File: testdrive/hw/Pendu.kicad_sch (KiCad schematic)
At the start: 26 parts, among them J2 Conn_01x04, J2 Conn_01x08, J3 Conn_01x05, J4 Conn_01x05, Q1 Si2301DS, SW1 Vib, U1 SPX3819M5-L-3-3, U2 STM32G030F6Px, U3 SPX3819M5-L-1-8, U4 BMI270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

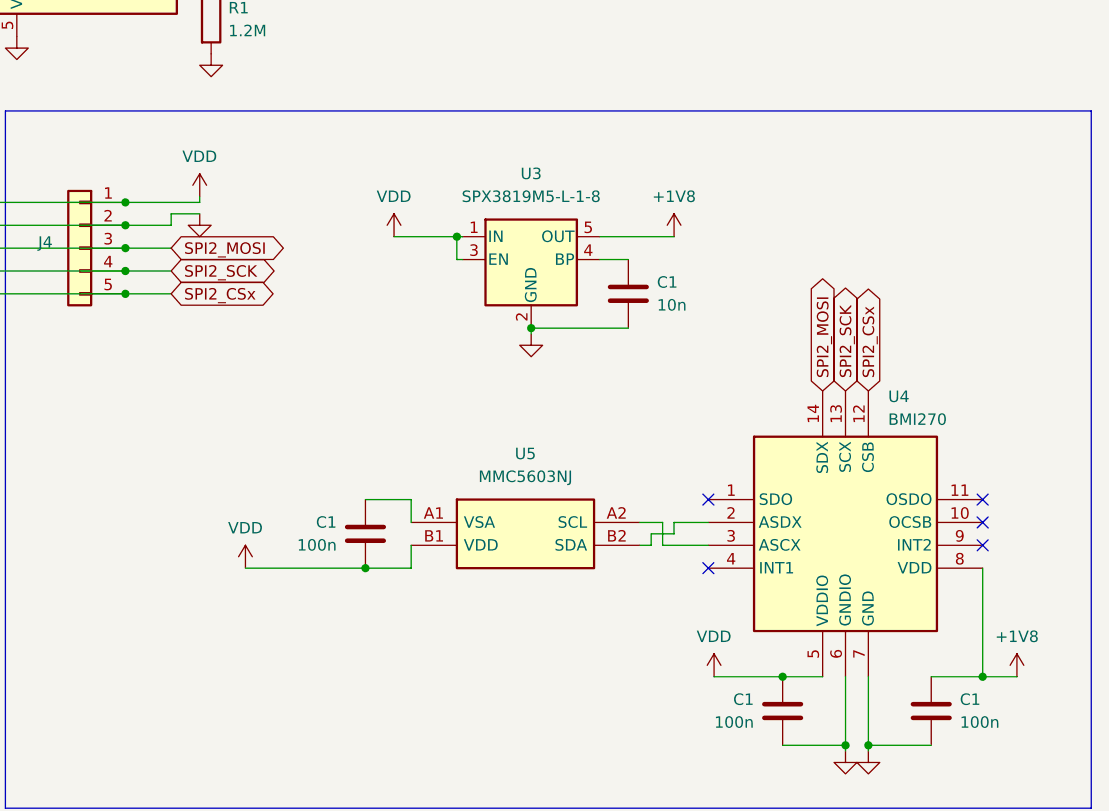
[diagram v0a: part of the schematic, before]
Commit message: Revise testdrive schematic, revert to unified VDD
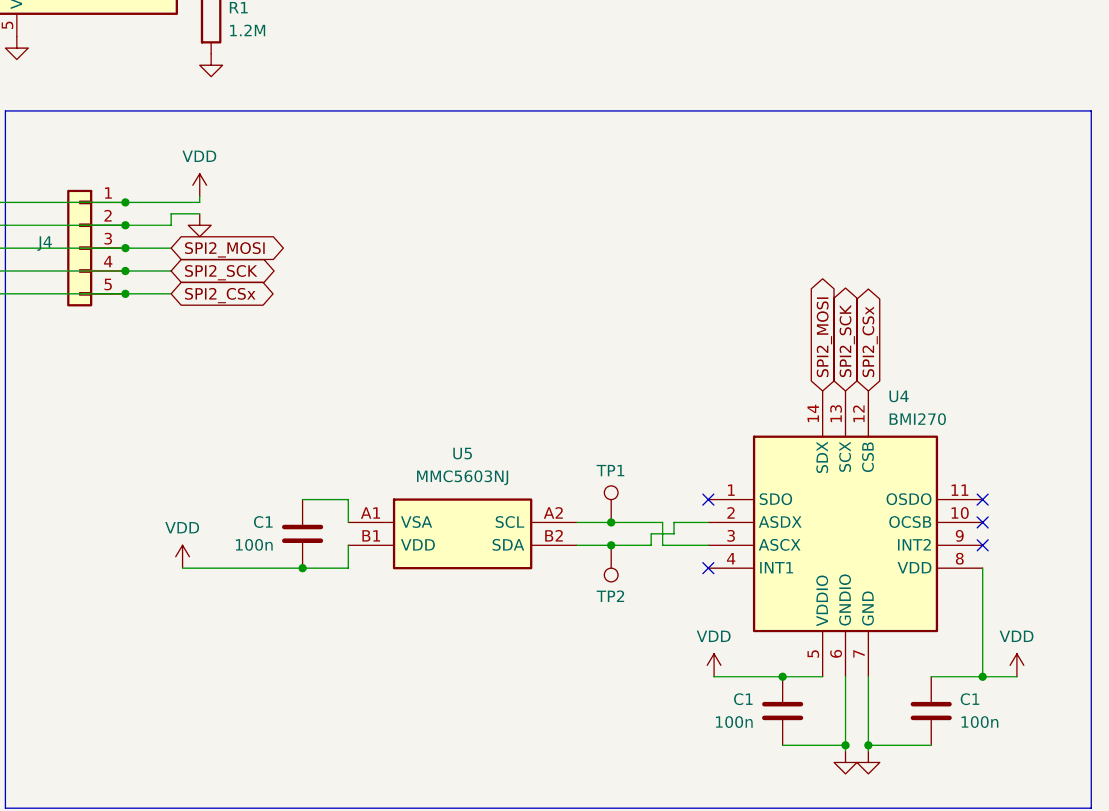
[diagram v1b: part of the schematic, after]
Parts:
- removed C1: 10n, Capacitor_SMD:C_0603_1608Metric, symbol Device:C
- removed U3: SPX3819M5-L-1-8, Package_TO_SOT_SMD:SOT-23-5, symbol Regulator_Linear:SPX3819M5-L-1-8
- added TP1, TP2: TestPoint, TestPoint:TestPoint_Pad_D1.5mm, symbol Connector:TestPoint
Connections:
- net +1V8 is gone; now on net VDD: C1.1, U4.8 (VDD)
- net at U4.3 (ASCX), U5.A2 (SCL): now also TP1.1
- net at U4.2 (ASDX), U5.B2 (SDA): now also TP2.1
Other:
- moved on the sheet: C1, U5

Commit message: Finish PCB layout and routing (schematic fix to-do)
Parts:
- C1: value 100n -> 2.2u
- renumbered U4 to U3, U5 to U4
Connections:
- net GND: now also C1.1, U4.A1 (VSA)
- net SPI1_CSx: now also U2.10 (PA3); no longer U2.11 (PA4)
- net nRF_CE: now also U2.11 (PA4); no longer U2.10 (PA3)
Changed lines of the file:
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@@
   (junction (at 68.58 22.225) (diameter 0) (color 0 0 0 0)
+  )
+  (junction (at 180.975 140.97) (diameter 0) (color 0 0 0 0)
   )
   (junction (at 215.265 146.05) (diameter 0) (color 0 0 0 0)
@@
     (stroke (width 0) (type default))
   )
+  (wire (pts (xy 167.64 140.97) (xy 180.975 140.97))
+    (stroke (width 0) (type default))
+  )
   (wire (pts (xy 222.25 143.51) (xy 226.06 143.51))
     (stroke (width 0) (type default))
@@
     )
   )
-  (global_label "SPI1_CSx" (shape bidirectional) (at 169.545 64.135 0) (fields_autoplaced)
-    (effects (font (size 1.27 1.27)) (justify left))
-    (property "Intersheetrefs" "${INTERSHEET_REFS}" (at 182.4105 64.135 0)
-      (effects (font (size 1.27 1.27)) (justify left) hide)
-    )
-  )
   (global_label "PWR_LATCH" (shape bidirectional) (at 52.07 33.02 270) (fields_autoplaced)
     (effects (font (size 1.27 1.27)) (justify right))
@@
     )
   )
-  (global_label "nRF_CE" (shape bidirectional) (at 169.545 61.595 0) (fields_autoplaced)
-    (effects (font (size 1.27 1.27)) (justify left))
-    (property "Intersheetrefs" "${INTERSHEET_REFS}" (at 180.5357 61.595 0)
-      (effects (font (size 1.27 1.27)) (justify left) hide)
-    )
-  )
   (global_label "SPI2_CSx" (shape bidirectional) (at 166.37 118.11 0) (fields_autoplaced)
     (effects (font (size 1.27 1.27)) (justify left))
     (property "Intersheetrefs" "${INTERSHEET_REFS}" (at 179.2355 118.11 0)
+      (effects (font (size 1.27 1.27)) (justify left) hide)
+    )
+  )
+  (global_label "nRF_CE" (shape bidirectional) (at 169.545 64.135 0) (fields_autoplaced)
+    (effects (font (size 1.27 1.27)) (justify left))
+    (property "Intersheetrefs" "${INTERSHEET_REFS}" (at 180.5357 64.135 0)
       (effects (font (size 1.27 1.27)) (justify left) hide)
     )
@@
     )
   )
+  (global_label "SPI1_CSx" (shape bidirectional) (at 169.545 61.595 0) (fields_autoplaced)
+    (effects (font (size 1.27 1.27)) (justify left))
+    (property "Intersheetrefs" "${INTERSHEET_REFS}" (at 182.4105 61.595 0)
+      (effects (font (size 1.27 1.27)) (justify left) hide)
+    )
+  )
   (global_label "SPI1_CK" (shape bidirectional) (at 97.155 118.11 0) (fields_autoplaced)
     (effects (font (size 1.27 1.27)) (justify left))
@@
       (effects (font (size 1.27 1.27)) (justify left))
     )
-    (property "Value" "100n" (at 177.8 146.05 0)
+    (property "Value" "2.2u" (at 177.8 146.05 0)
       (effects (font (size 1.27 1.27)) (justify left))
     )
@@
   )
   (symbol (lib_id "power:VDD") (at 167.64 148.59 0) (unit 1)
-    (in_bom yes) (on_board yes) (dnp no) (fields_autoplaced)
+    (in_bom yes) (on_board yes) (dnp no)
     (property "Reference" "#PWR02" (at 167.64 152.4 0)
       (effects (font (size 1.27 1.27)) hide)
     )
-    (property "Value" "VDD" (at 167.64 144.145 0)
+    (property "Value" "VDD" (at 164.465 147.32 0)
       (effects (font (size 1.27 1.27)))
     )
@@
         (path "/b391cdd2-d886-4ef4-8596-8b3281b3cce1"
           (reference "TP2") (unit 1)
+        )
+      )
+    )
+  )
+  (symbol (lib_id "power:GND") (at 167.64 140.97 0) (unit 1)
+    (in_bom yes) (on_board yes) (dnp no) (fields_autoplaced)
+    (property "Reference" "#PWR01" (at 167.64 147.32 0)
+      (effects (font (size 1.27 1.27)) hide)
+    )
+    (property "Value" "GND" (at 167.64 145.415 0)
+      (effects (font (size 1.27 1.27)) hide)
+    )
+    (property "Footprint" "" (at 167.64 140.97 0)
+      (effects (font (size 1.27 1.27)) hide)
+    )
+    (property "Datasheet" "" (at 167.64 140.97 0)
+      (effects (font (size 1.27 1.27)) hide)
+    )
+    (pin "1")
+    (instances
+      (project "ResSensor_R2"
+        (path "/4fdceb17-4902-4163-aeee-a94f9382439a"
+          (reference "#PWR01") (unit 1)
+        )
+      )
+      (project "Pendu"
+        (path "/b391cdd2-d886-4ef4-8596-8b3281b3cce1"
+          (reference "#PWR016") (unit 1)
         )
       )
@@
   (symbol (lib_id "Pendu_symbols:MMC5603NJ") (at 186.055 143.51 0) (unit 1)
     (in_bom yes) (on_board yes) (dnp no) (fields_autoplaced)
-    (property "Reference" "U5" (at 198.755 135.89 0)
+    (property "Reference" "U4" (at 198.755 135.89 0)
       (effects (font (size 1.27 1.27)))
     )
@@
       (project "Pendu"
         (path "/b391cdd2-d886-4ef4-8596-8b3281b3cce1"
-          (reference "U5") (unit 1)
+          (reference "U4") (unit 1)
         )
       )
@@
   (symbol (lib_id "Pendu_symbols:BMI270") (at 226.06 140.97 0) (unit 1)
     (in_bom yes) (on_board yes) (dnp no) (fields_autoplaced)
-    (property "Reference" "U4" (at 246.0341 129.54 0)
+    (property "Reference" "U3" (at 246.0341 129.54 0)
       (effects (font (size 1.27 1.27)) (justify left))
     )
@@
       (project "Pendu"
         (path "/b391cdd2-d886-4ef4-8596-8b3281b3cce1"
-          (reference "U4") (unit 1)
-        )
-      )
+          (reference "U3") (unit 1)
+        )
+      )

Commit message: Fix circuit design, submit for fabrication
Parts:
- added Q2: Si2301DS, Package_TO_SOT_SMD:SOT-23, symbol Device:Q_PMOS_GSD
- added R1: 1.2M, Resistor_SMD:R_0603_1608Metric, symbol Device:R
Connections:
- net PWR_LATCH: now also U2.12 (PA5), Q2.1 (G), R1.2; no longer Q1.1 (G), R1.1, SW1.1
- net at Q1.3 (D), U1.1 (IN), U1.3 (EN): now also Q2.3 (D)
- net VA|BAT renamed VBAT
- net VBAT: now also Q2.2 (S), R1.1
- new net: Q1.1 (G), R1.1, SW1.1
- no-connect marks 11 -> 10
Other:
- moved on the sheet: C1, C2, C3, D2, J2, J3, J4, R1, R6, R7, R8, TP1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
